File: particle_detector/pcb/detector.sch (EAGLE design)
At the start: 25 parts, among them IC1 LT1807R

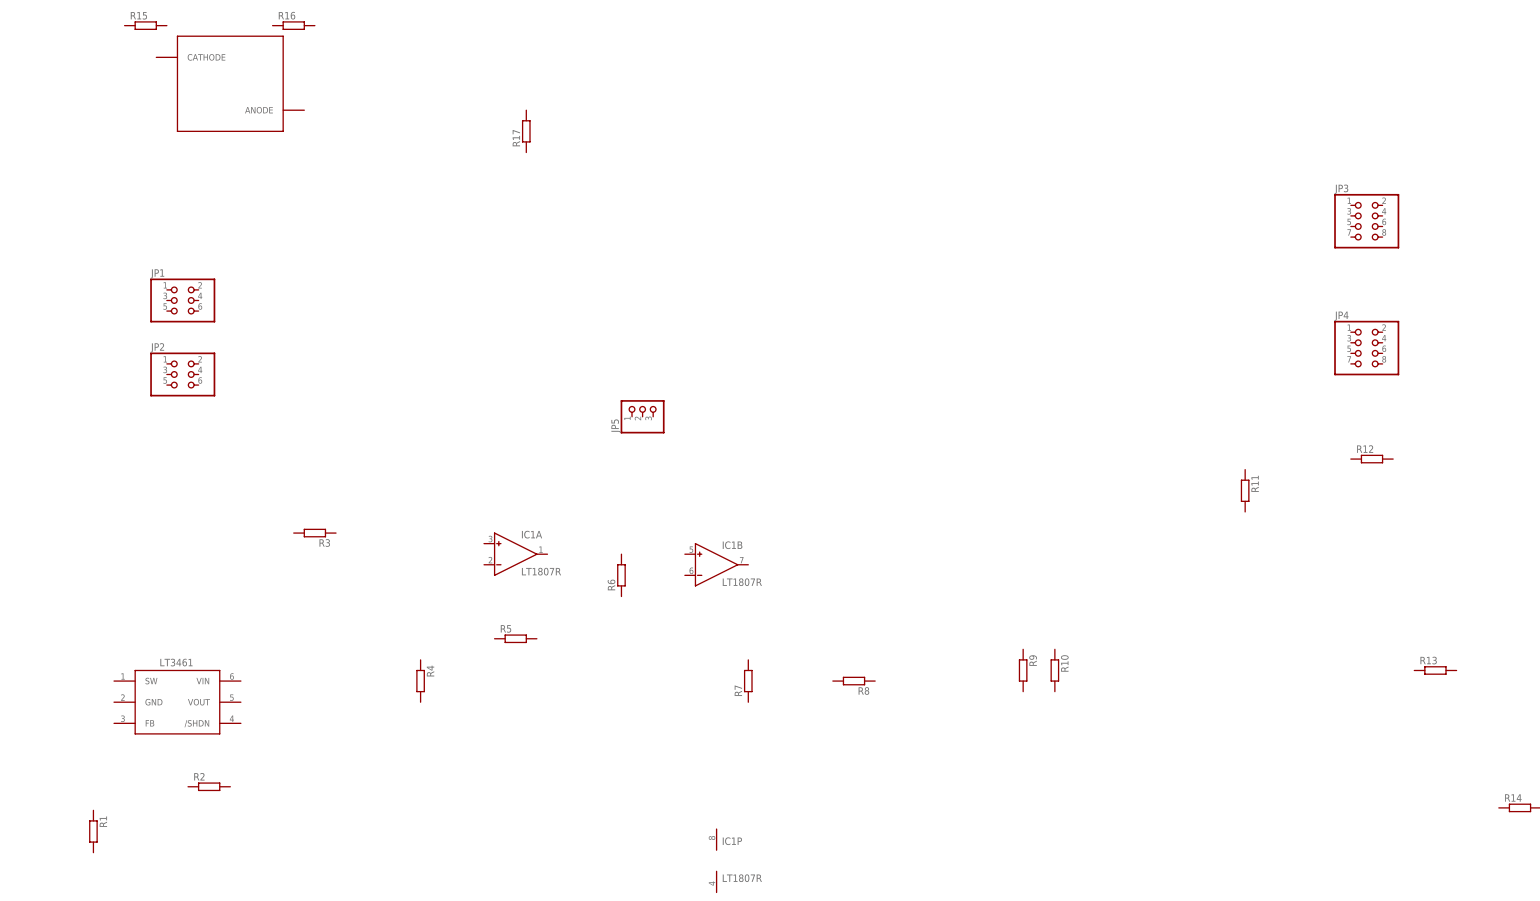
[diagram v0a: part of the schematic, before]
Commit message: complete SiPM and HV schs, partial completion of amplifier, hold schs
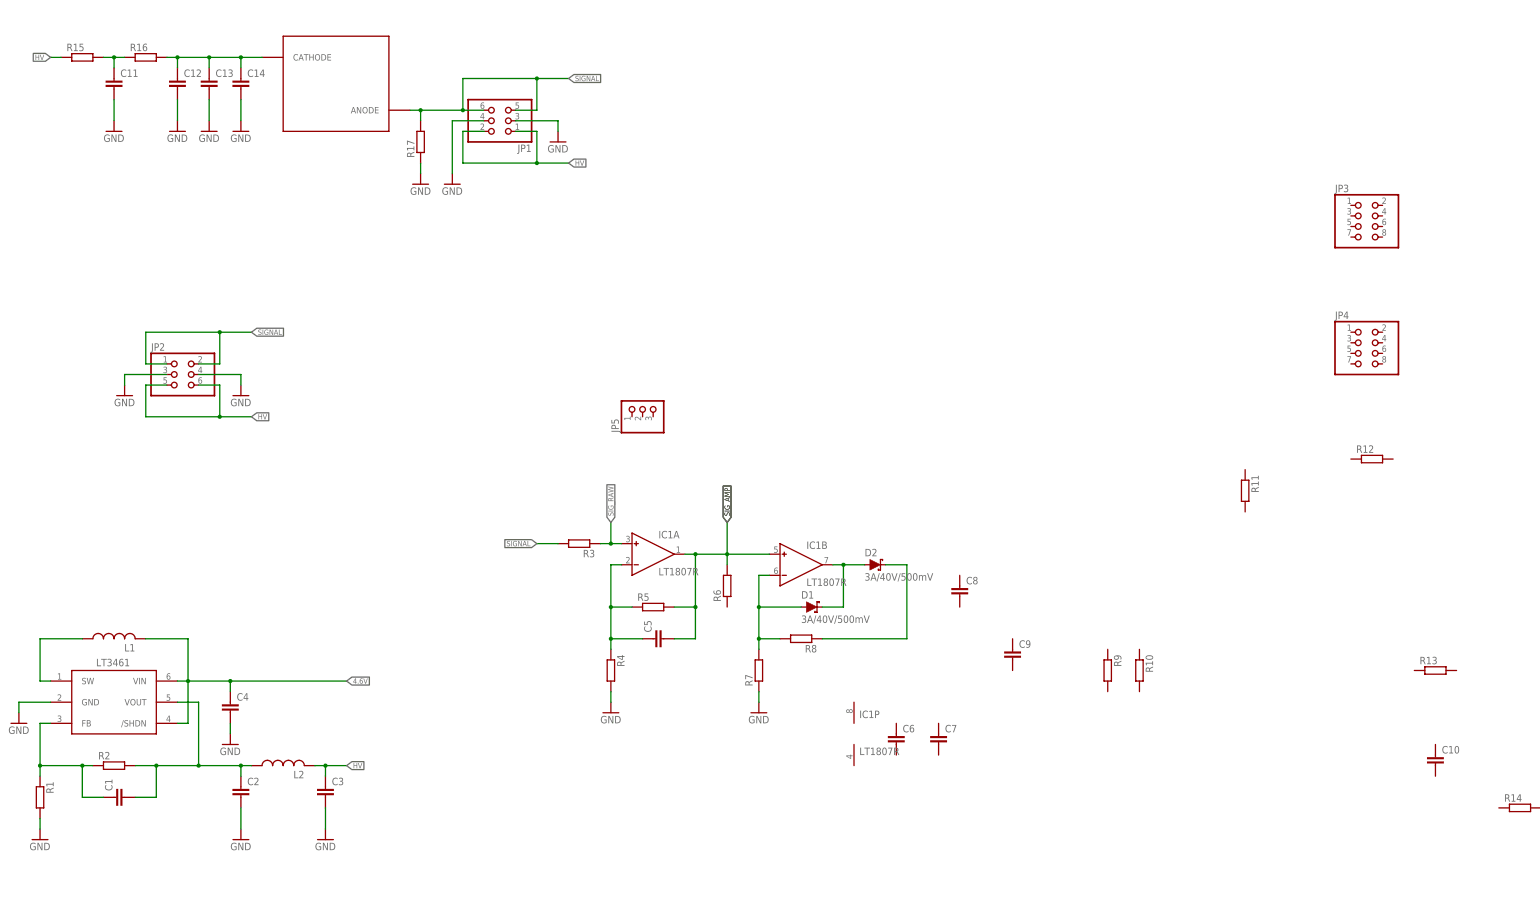
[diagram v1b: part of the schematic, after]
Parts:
- added C1, C10, C11, C12, C13, C14, C2, C3, C4, C5, C6, C7, C8, C9: (no value), rcl:C-EUC0805
- added D1, D2: 3A/40V/500mV, SparkFun-DiscreteSemi:DIODE-SCHOTTKY-B340A
- added L1, L2: (no value), rcl:L-USL2012C
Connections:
- new net 4.6V: C4.1, L1.2, U$1./SHDN, U$1.VIN
- new net GND: C11.2, C12.2, C13.2, C14.2, C2.2, C3.2, C4.2, JP1.3, JP1.4, JP2.3, JP2.4, R1.2, R17.1, R4.2, R7.1, U$1.GND
- new net HV: C3.1, JP1.1, JP1.2, JP2.5, JP2.6, L2.2, R15.1
- new net N$1: L1.1, U$1.SW
- new net N$2: D1.C, D2.A, IC1B.OUT
- new net N$3: C1.1, R1.1, R2.1, U$1.FB
- new net N$4: D1.A, IC1B.IN-, R7.2, R8.2
- new net N$5: C12.1, C13.1, C14.1, R16.2, U$2.CATHODE
- new net N$6: C11.1, R15.2, R16.1
- new net N$7: C1.2, C2.1, L2.1, R2.2, U$1.VOUT
- new net N$8: C5.1, IC1A.IN-, R4.1, R5.1
- new net N$9: D2.C, R8.1
- new net SIGNAL: JP1.5, JP1.6, JP2.1, JP2.2, R17.2, R3.2, U$2.ANODE
- new net SIG_AMP: C5.2, IC1A.OUT, IC1B.IN+, R5.2, R6.2
- new net SIG_RAW: IC1A.IN+, R3.1
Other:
- moved on the sheet: IC1A, IC1B, IC1P, JP1, R1, R10, R15, R16, R17, R2, R3, R4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

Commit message: complete first pass of sch
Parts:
- removed C14: (no value), rcl:C-EUC0805
- removed JP3, JP4: (no value), pinhead:PINHD-2X4
- removed R14, R15, R16, R17: (no value), rcl:R-EU_M0805
- added IC4: TEENSY_3.2_NO_BOTTOM, personal:TEENSY_3.2_NO_BOTTOM
- D1, D2: value 3A/40V/500mV -> B340A
- renumbered U$1 to IC3, U$2 to IC2
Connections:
- removed net 4.6V: C4.1, IC3./SHDN, IC3.VIN, L1.2
- new net N$10: IC4.14/A0, R10.2
- new net SIG_PEAK: C8.1, C9.1, D2.C, JP5.3, R8.2
- new net VCC: C4.1, C6.1, C7.1, IC1P.V+, IC3./SHDN, IC3.VIN, IC4.VIN, L1.1
- net GND: now also C10.2, C6.2, C7.2, C8.2, IC1P.V-, IC4.GND, R1.1, R13.1, R4.1, R6.1, R9.1; no longer C14.2, R1.2, R17.1, R4.2
- net HV: now also L2.1, R11.1; no longer L2.2, R15.1
- net N$1: now also L1.2; no longer L1.1
- net N$3: now also R1.2; no longer R1.1
- net N$4: now also R8.1; no longer R8.2
- net N$5: now also C11.1, R12.2; no longer C14.1, R16.2
- net N$6: now also C10.1, R11.2, R12.1; no longer C11.1, R15.2, R16.1
- net N$7: now also L2.2; no longer L2.1
- net N$8: now also R4.2; no longer R4.1
- net N$9: now also C9.2, R10.1, R9.2; no longer D2.C, R8.1
- net SIGNAL: now also R13.2, R3.1; no longer R17.2, R3.2
- net SIG_AMP: now also JP5.2
- net SIG_RAW: now also JP5.1, R3.2; no longer R3.1
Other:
- note added: "01"
- note added: "Amplification"
- note added: "Author: Kristof Aldenderfer Forked from Cosmic Watch v2"
- note added: "DC-DC Booster"
- note added: "Microcontroller"
- note added: "Peak Detection and Hold"
- note added: "SiPM Connection"
- note added: "SiPM PCB"
- note added: "Touch Points"
- moved on the sheet: C10, C11, C12, C13, C6, C7, C8, C9, IC1B, IC1P, JP5, L1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
